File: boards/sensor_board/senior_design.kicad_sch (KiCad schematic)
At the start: 16 parts, among them J1 Conn_01x04, U11 UA741CP, U3 AD620, U4 AD630ARZ, U7 UA741CP

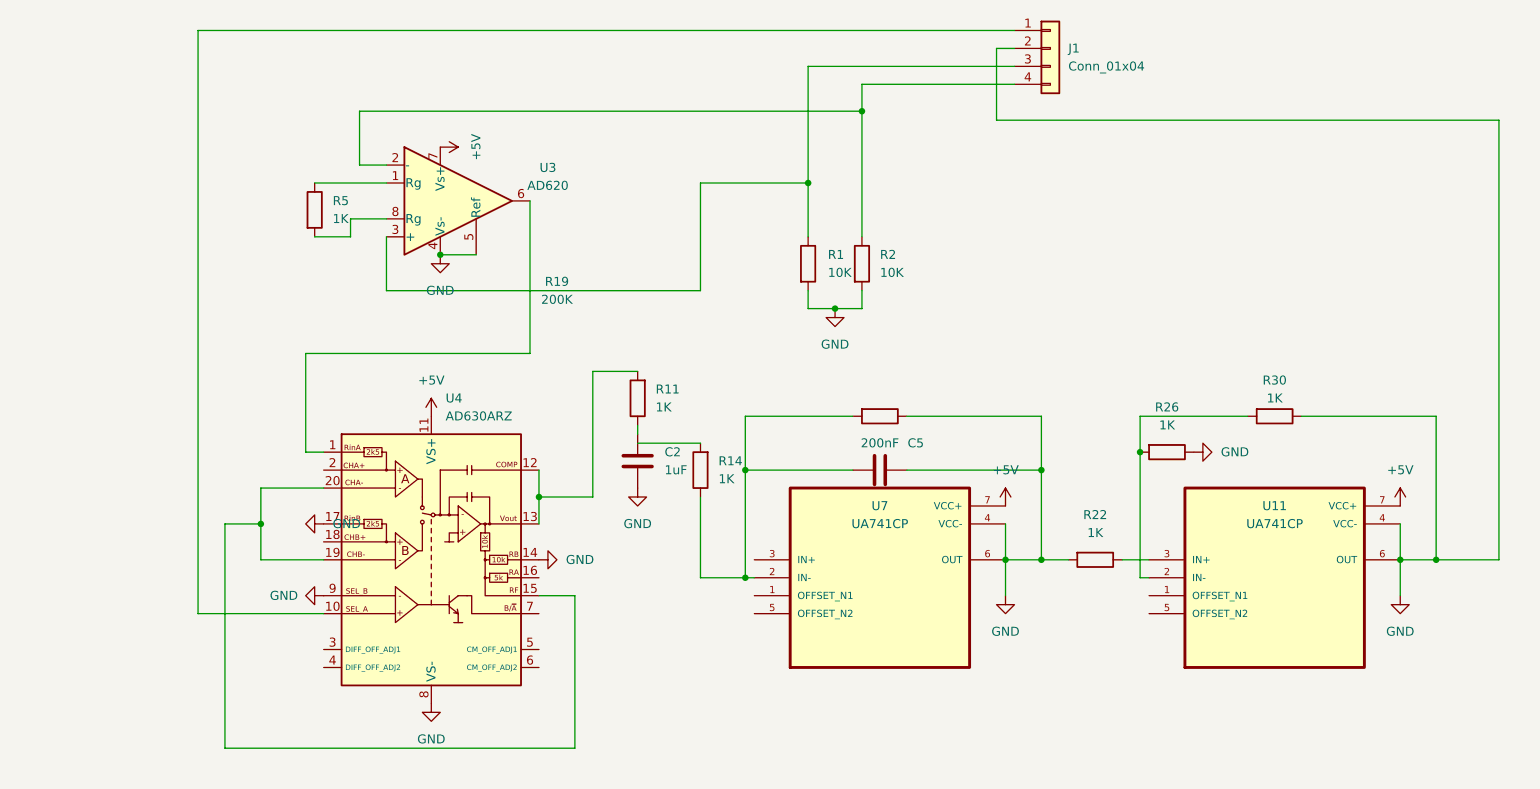
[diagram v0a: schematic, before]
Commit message: finished PCB for sensor board
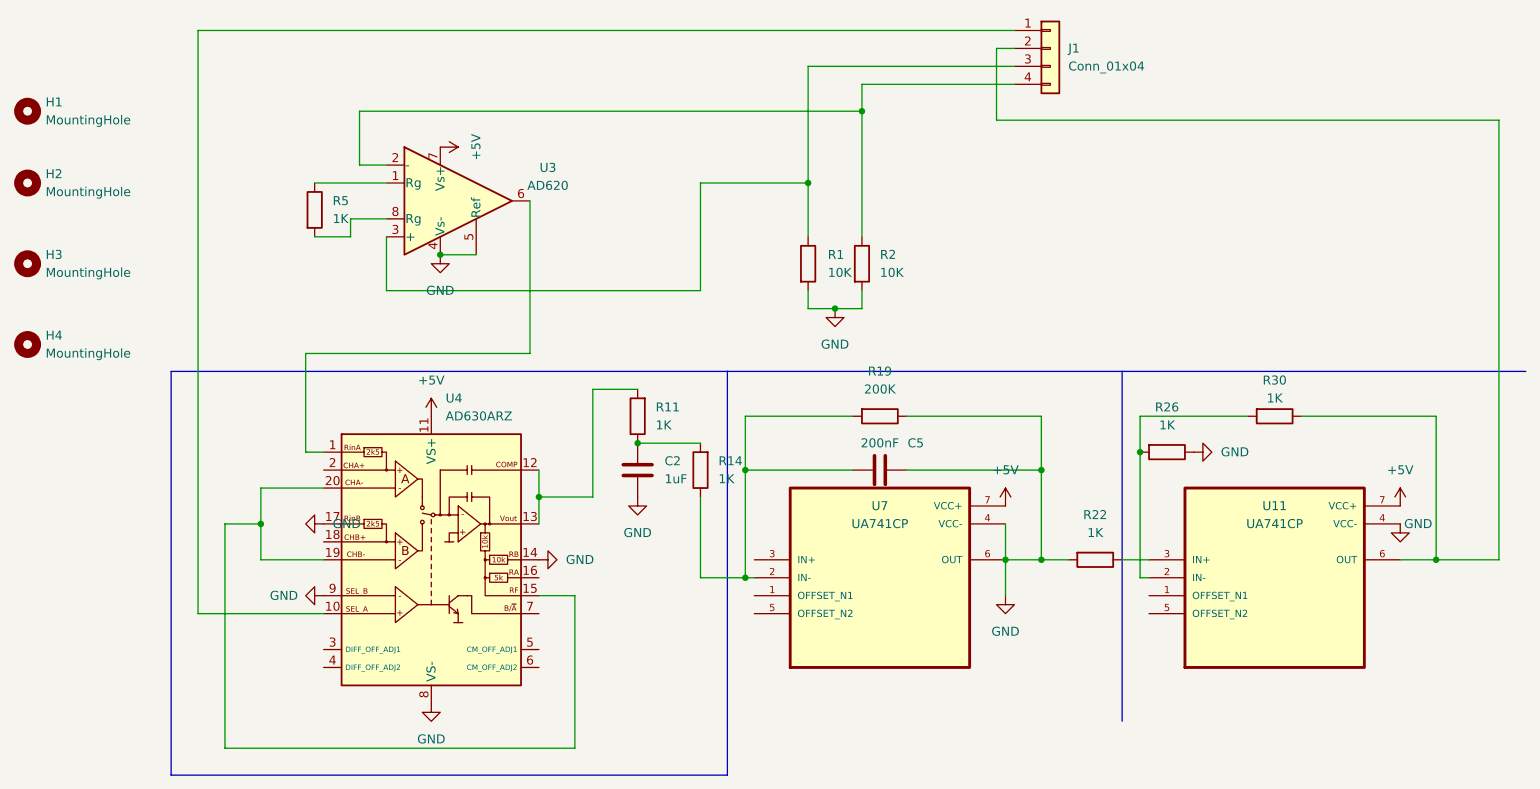
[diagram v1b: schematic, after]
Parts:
- added H1, H2, H3, H4: MountingHole, MountingHole:MountingHole_3.2mm_M3, symbol Mechanical:MountingHole
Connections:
- net GND: no longer J1.2 (Pin_2), R30.1, U11.6 (OUT)
- net at R14.2: now also C2.2, R11.1
- new net: J1.2 (Pin_2), R30.1, U11.6 (OUT)
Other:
- moved on the sheet: C2, R11
